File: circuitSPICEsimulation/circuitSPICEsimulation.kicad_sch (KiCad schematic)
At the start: 31 parts, among them U1 ${SIM.PARAMS}, U2 ${SIM.PARAMS}, U3 ${SIM.PARAMS}, U4 ${SIM.PARAMS}, U6 ${SIM.PARAMS}

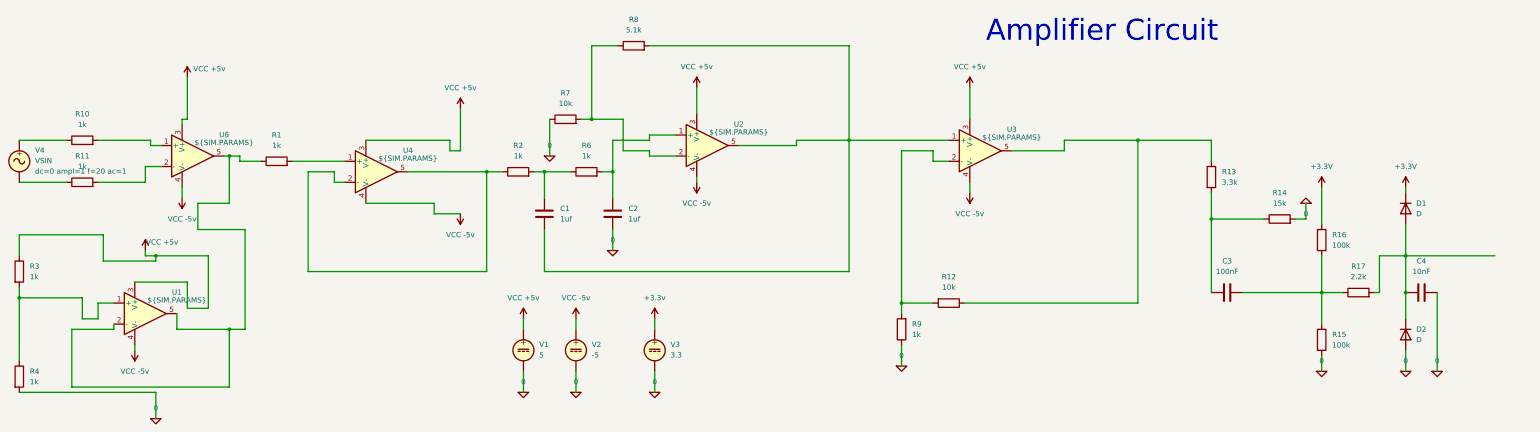
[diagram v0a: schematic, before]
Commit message: Created the PCB, still need to make changes depending on testing on breadboard
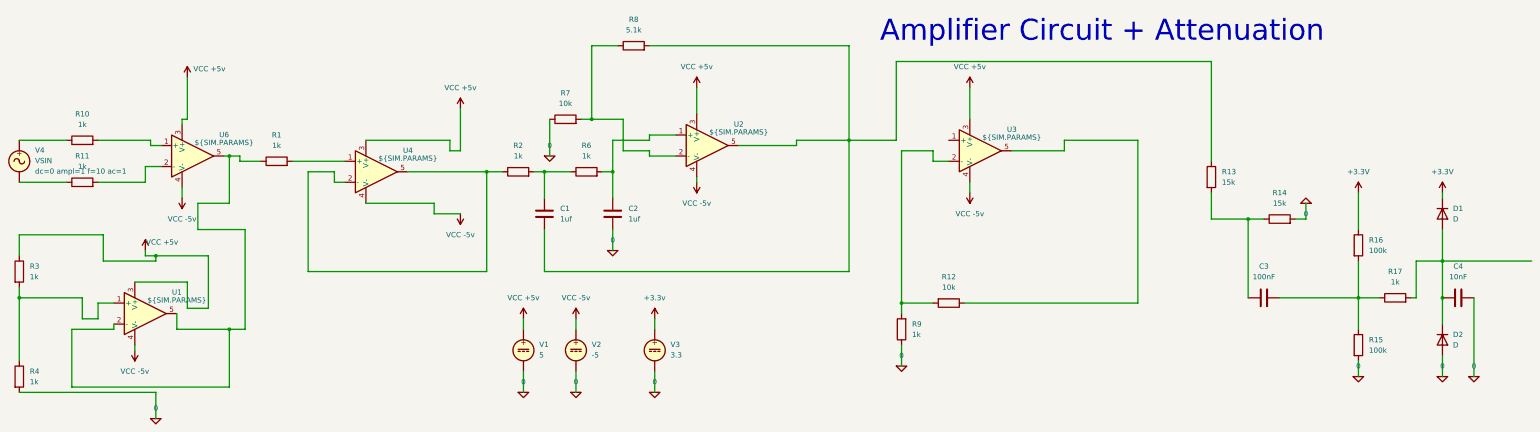
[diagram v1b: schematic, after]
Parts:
- R13: value 3.3k -> 15k
- R17: value 2.2k -> 1k
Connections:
- net at C1.2, R8.2, U2.5: now also R13.1; no longer U3.1 (+)
- net at R12.1, U3.5: no longer R13.1
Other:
- note added: "Amplifier Circuit + Attenuation"
- note removed: "Amplifier Circuit"
- moved on the sheet: C3, C4, D1, D2, R15, R16, R17
